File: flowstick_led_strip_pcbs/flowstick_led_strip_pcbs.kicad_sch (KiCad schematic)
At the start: 2 parts, among them J1 LED, J2 LED

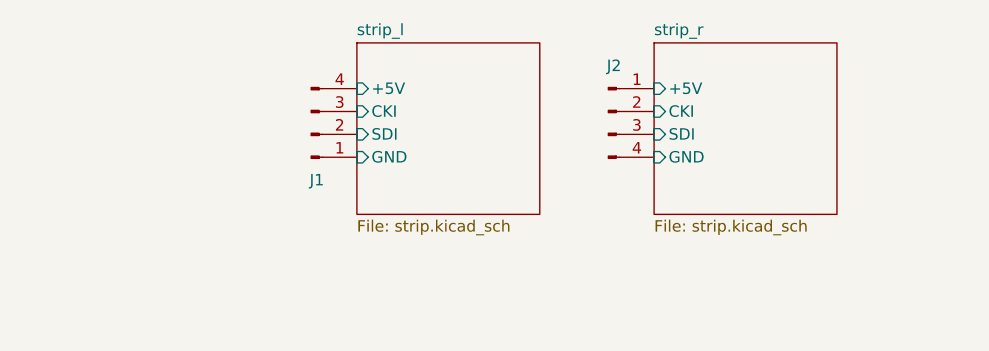
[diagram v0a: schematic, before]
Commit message: work on rev2 + panelize LED strips
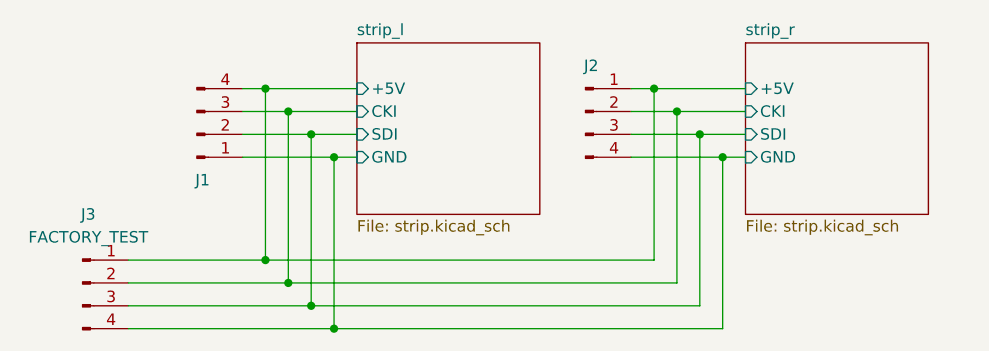
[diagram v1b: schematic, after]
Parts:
- added J3: FACTORY_TEST, Connector_PinHeader_2.54mm:PinHeader_1x04_P2.54mm_Vertical, symbol Connector:Conn_01x04_Pin
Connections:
- net strip_r/+5V is gone; now on net strip_l/+5V: J2.1 (Pin_1)
- net strip_r/CKI is gone; now on net strip_l/CKI: J2.2 (Pin_2)
- net strip_r/GND is gone; now on net strip_l/GND: J2.4 (Pin_4)
- net strip_r/SDI is gone; now on net strip_l/SDI: J2.3 (Pin_3)
- net strip_l/+5V: now also J3.1 (Pin_1)
- net strip_l/CKI: now also J3.2 (Pin_2)
- net strip_l/GND: now also J3.4 (Pin_4)
- net strip_l/SDI: now also J3.3 (Pin_3)
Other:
- moved on the sheet: J1, J2
